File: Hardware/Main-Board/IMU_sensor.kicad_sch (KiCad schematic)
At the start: 5 parts, among them J3 MSD-10-C

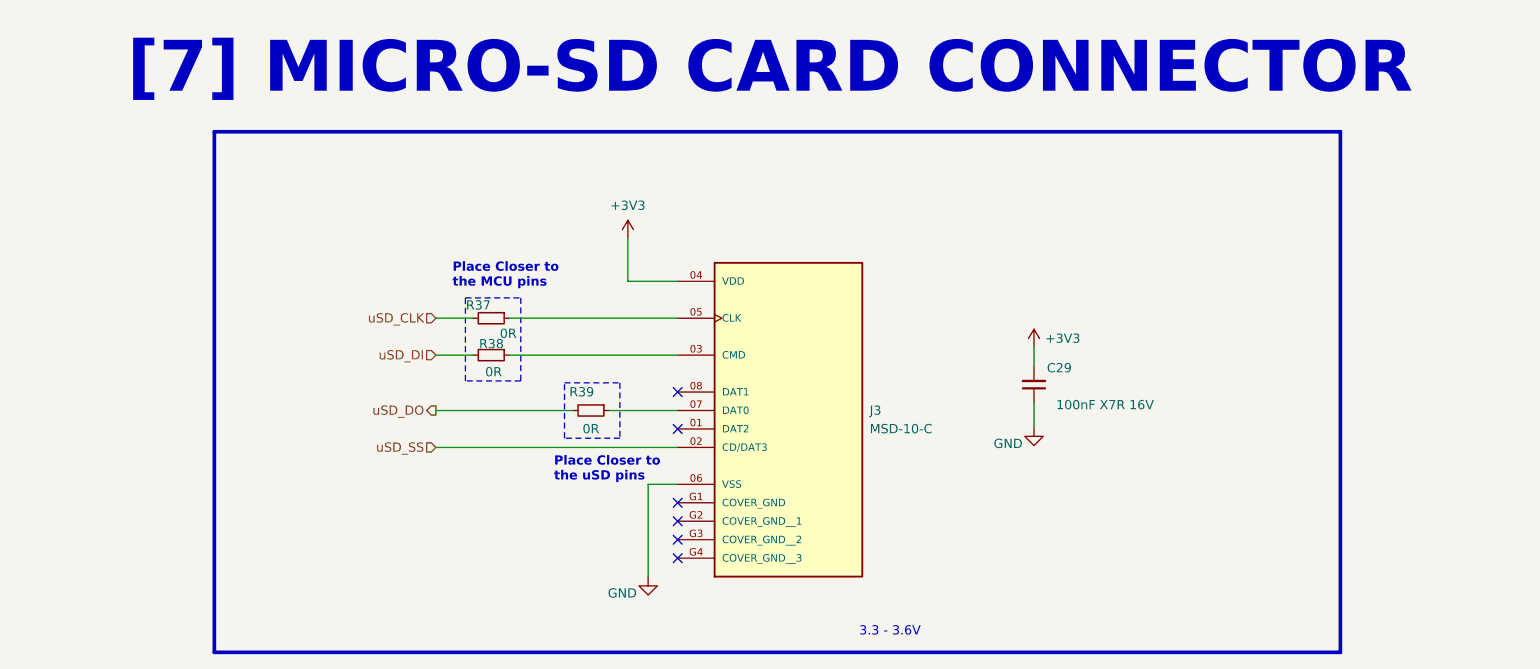
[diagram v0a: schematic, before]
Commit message: Done with main board design, and camera interconnect in progress
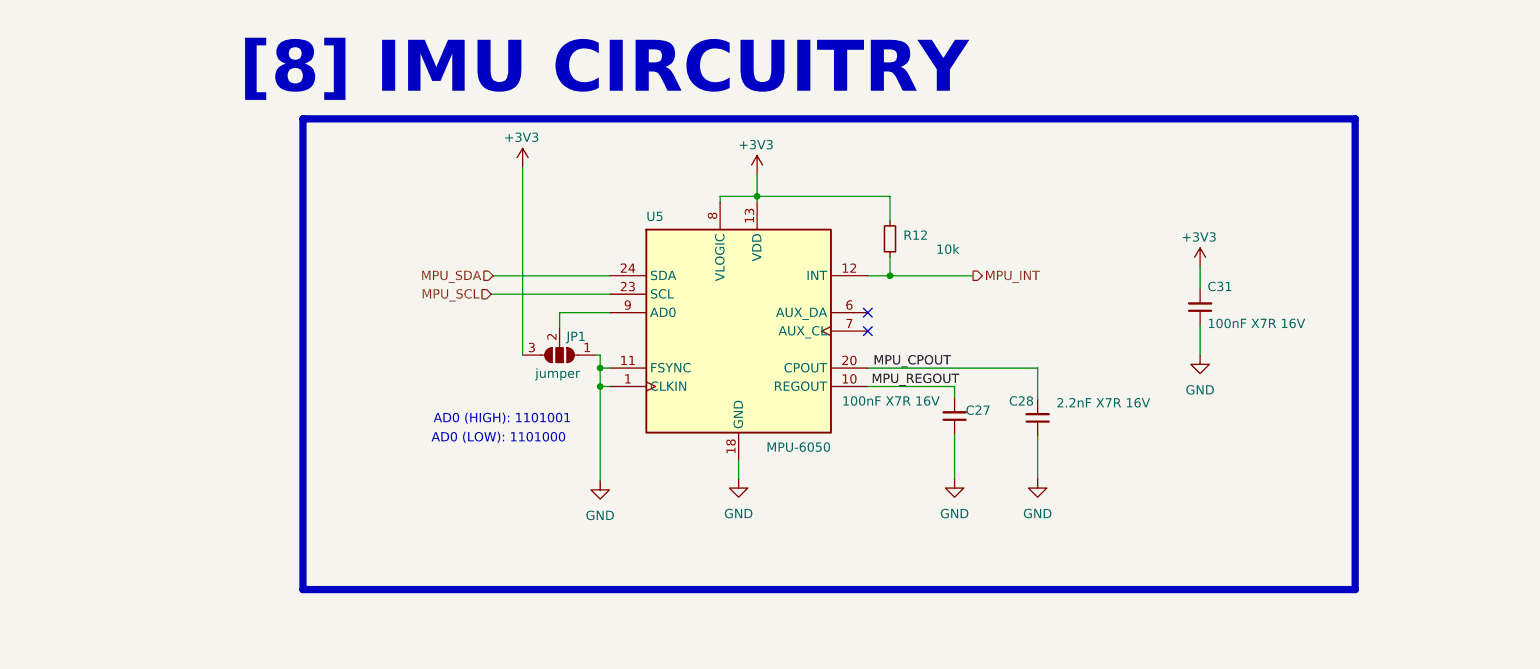
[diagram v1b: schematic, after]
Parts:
- removed C29: 100nF X7R 16V, Capacitor_SMD:C_0402_1005Metric, symbol Device:C_Small
- removed J3: MSD-10-C, MSD_10_C:CUI_MSD-10-C, symbol MSD-10-C:MSD-10-C
- removed R37, R38, R39: 0R, Resistor_SMD:R_0402_1005Metric, symbol Device:R_Small
- added C27, C31: 100nF X7R 16V, Capacitor_SMD:C_0402_1005Metric, symbol Device:C_Small
- added C28: 2.2nF X7R 16V, Capacitor_SMD:C_0402_1005Metric, symbol Device:C_Small
- added JP1: jumper, Jumper:SolderJumper-3_P1.3mm_Bridged12_RoundedPad1.0x1.5mm, symbol Jumper:SolderJumper_3_Open
- added R12: 10k, Resistor_SMD:R_0402_1005Metric, symbol Device:R_Small
- added U5: MPU-6050, Sensor_Motion:InvenSense_QFN-24_4x4mm_P0.5mm, symbol Sensor_Motion:MPU-6050
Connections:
- net +3V3: now also C31.2, JP1.3 (B), R12.2, U5.13 (VDD), U5.8 (VLOGIC)
- net GND: now also C27.1, C28.1, C31.1, JP1.1 (A), U5.1 (CLKIN), U5.11 (FSYNC), U5.18 (GND)
- new net: JP1.2 (C), U5.9 (AD0)
- new net MPU_CPOUT: C28.2, U5.20 (CPOUT)
- new net MPU_INT: R12.1, U5.12 (INT)
- new net MPU_REGOUT: C27.2, U5.10 (REGOUT)
- new net MPU_SCL: U5.23 (SCL)
- new net MPU_SDA: U5.24 (SDA)
- no-connect marks 6 -> 2
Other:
- note added: "AD0 (HIGH): 1101001"
- note added: "AD0 (LOW): 1101000"
- note added: "[8] IMU CIRCUITRY"
- note removed: "3.3 - 3.6V"
- note removed: "Place Closer to the MCU pins"
- note removed: "Place Closer to the uSD pins"
- note removed: "[7] MICRO-SD CARD CONNECTOR"
